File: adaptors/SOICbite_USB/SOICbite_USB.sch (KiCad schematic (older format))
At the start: 3 parts, among them J1 USB_B_Micro, J2 2x4_IDC, J3 Conn_01x05

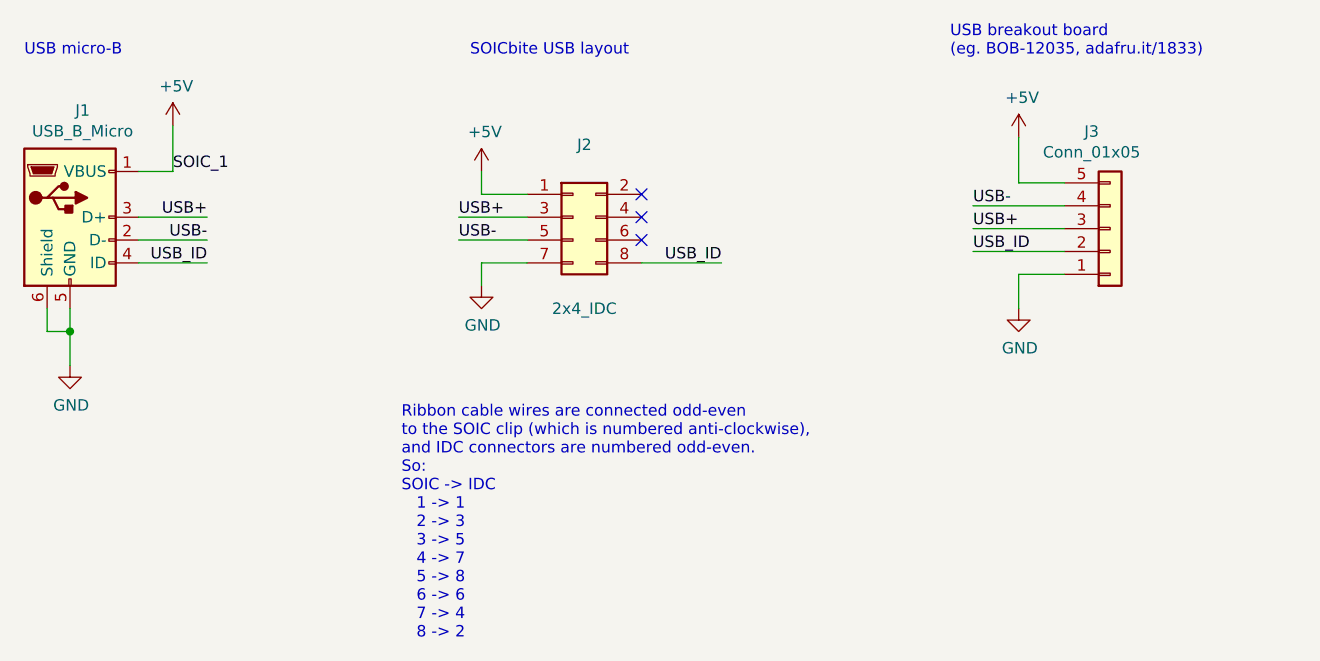
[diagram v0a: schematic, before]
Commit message: rev2 layout, moved USB_ID to SOICbite pin 8
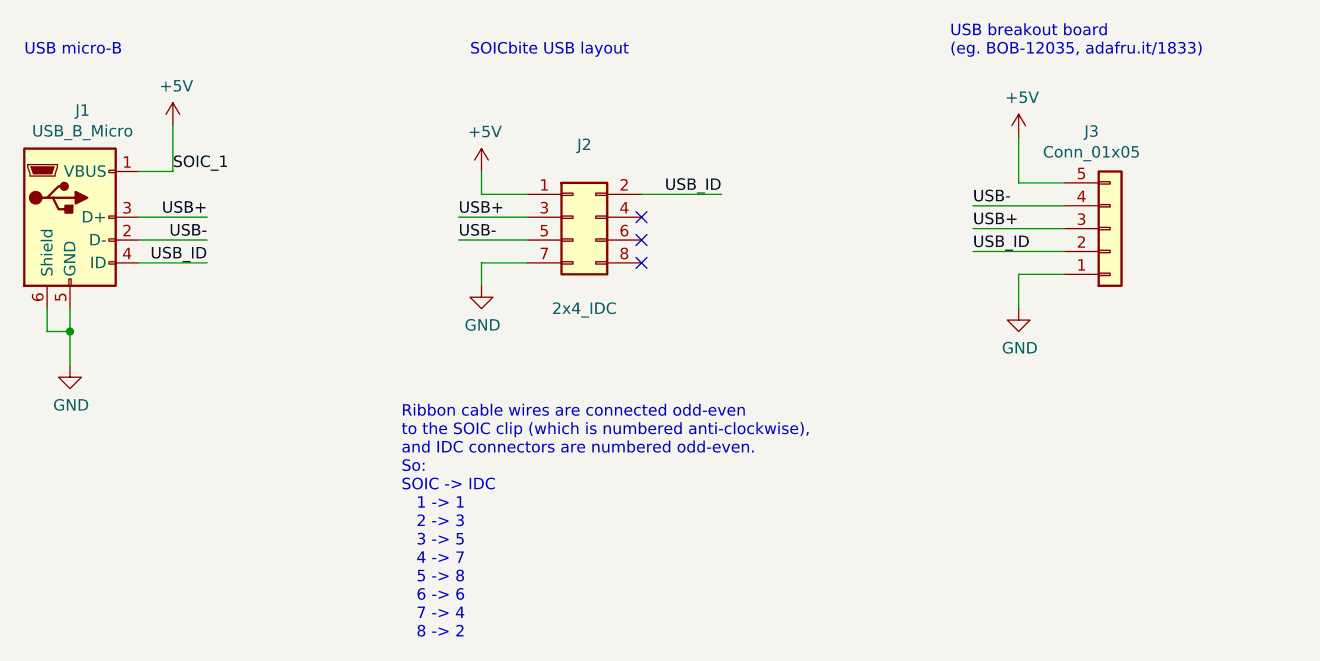
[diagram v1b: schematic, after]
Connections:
- net USB_ID: now also J2.2 (Pin_2); no longer J2.8 (Pin_8)
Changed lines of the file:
@@
 Wire Wire Line
 	3000 2300 3300 2300
-Text Label 5550 2300 2    50   ~ 0
+Text Label 5550 2000 2    50   ~ 0
 USB_ID
 $Comp
@@
 SOIC_1
 Wire Wire Line
-	5550 2300 5200 2300
+	5550 2000 5200 2000
 Wire Wire Line
 	4400 2100 4700 2100
@@
 Wire Wire Line
 	4400 2200 4700 2200
-NoConn ~ 5200 2000
+NoConn ~ 5200 2300
 NoConn ~ 5200 2100
 NoConn ~ 5200 2200

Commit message: revised pinout, D- should be by Vcc
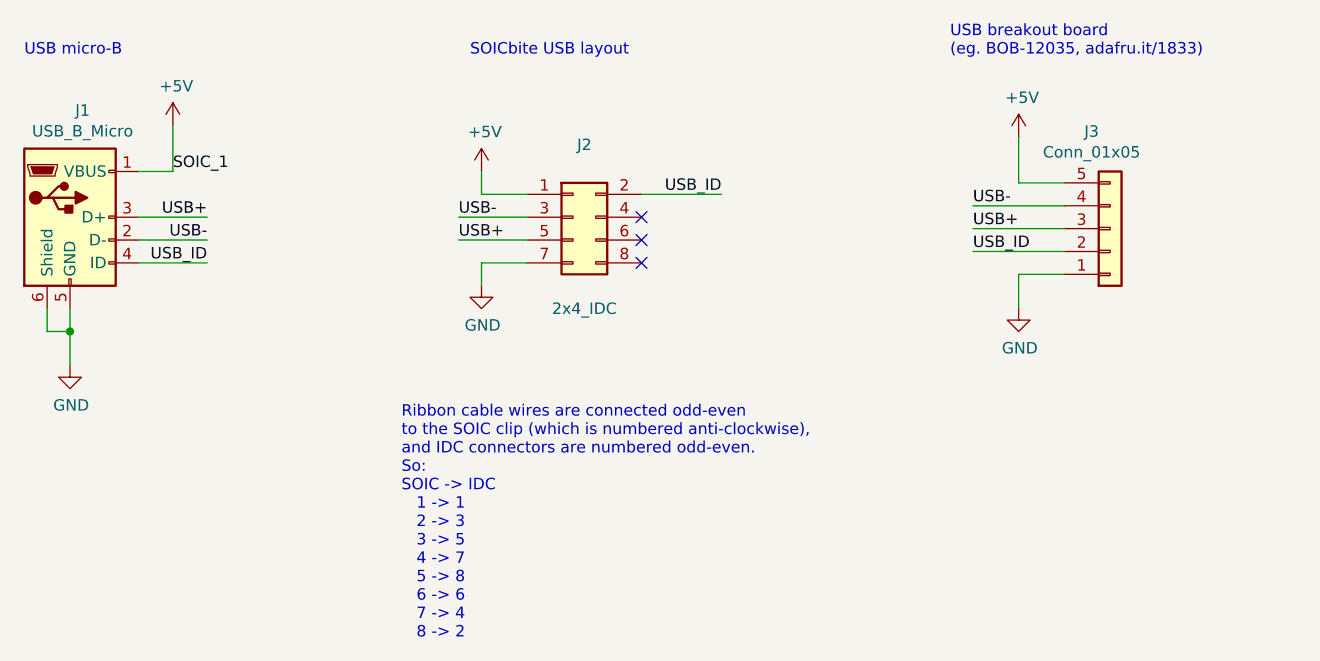
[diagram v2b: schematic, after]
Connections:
- net USB+: now also J2.5 (Pin_5); no longer J2.3 (Pin_3)
- net USB-: now also J2.3 (Pin_3); no longer J2.5 (Pin_5)
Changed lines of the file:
@@
 Text Label 3300 2200 2    50   ~ 0
 USB-
+Text Label 4400 2200 0    50   ~ 0
+USB+
 Text Label 4400 2100 0    50   ~ 0
-USB+
-Text Label 4400 2200 0    50   ~ 0
 USB-
 Wire Wire Line
